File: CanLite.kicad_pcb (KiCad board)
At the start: 2 copper layers, 40 x 53.6 mm, 42 parts, among them J1 12V, J2 CAN, J3 VOLTLINK, J4 Conn_01x03, U1 LMR14006, U2 ESP32-WROOM-32D, U3 SN65HVD231, U4 BTS452T, U5 BTS452T

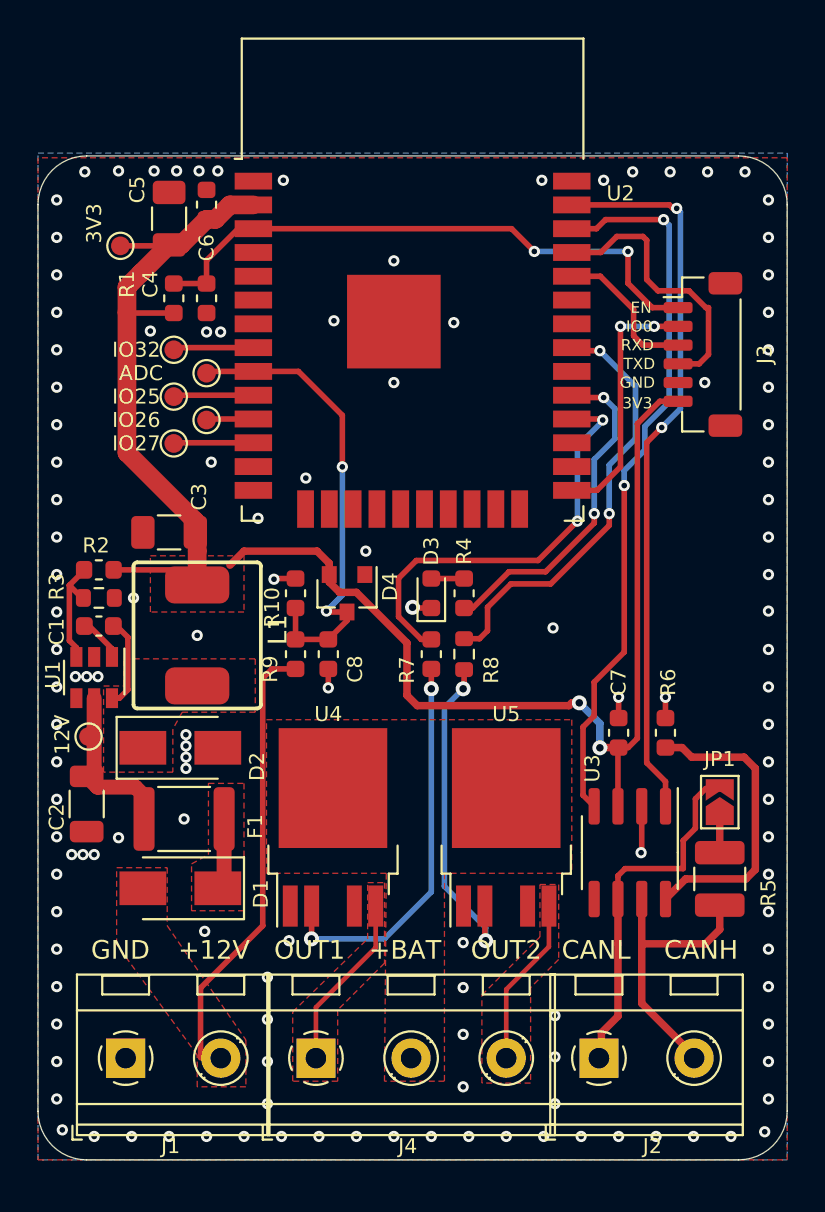
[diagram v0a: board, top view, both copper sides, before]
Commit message: Removed high side drivers, added SD card reader
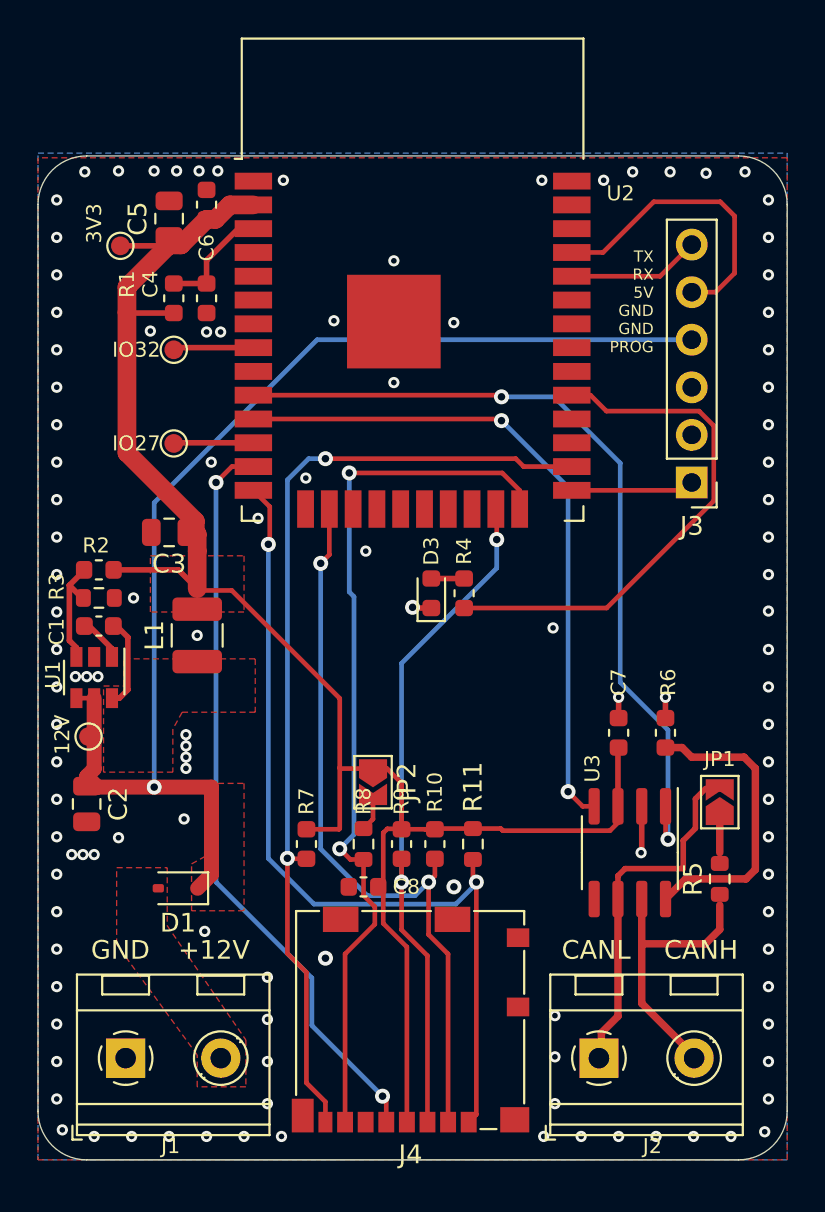
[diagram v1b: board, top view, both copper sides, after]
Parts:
- removed D2: SS14, Diode_SMD:D_SMA
- removed D4: BAS40-04, Package_TO_SOT_SMD:SOT-23
- removed F1: 0.5A, Fuse:Fuse_1812_4532Metric
- removed TP3: IO25, TestPoint:TestPoint_Pad_D1.0mm
- removed TP4: IO26, TestPoint:TestPoint_Pad_D1.0mm
- removed TP7: ADC, TestPoint:TestPoint_Pad_D1.0mm
- removed U4, U5: BTS452T, Package_TO_SOT_SMD:TO-252-4
- removed V1: VOLTLOG_LOGO, Voltlog:voltlog_mask_3mm
- added JP2: NO, Jumper:SolderJumper-2_P1.3mm_Open_TrianglePad1.0x1.5mm, F.Cu at (119.9, 84.8)
- added R11: na, Resistor_SMD:R_0603_1608Metric, F.Cu at (125.2, 88.1)
- C2, C3, C5: footprint Capacitor_SMD:C_1206_3216Metric -> Capacitor_SMD:C_0805_2012Metric
- D1: value SS14 -> 1N4148; footprint Diode_SMD:D_SMA -> Diode_SMD:D_SOD-323
- J3: value VOLTLINK -> ~; footprint Connector_JST:JST_SH_BM06B-SRSS-TB_1x06-1MP_P1.00mm_Vertical -> Connector_PinHeader_2.54mm:PinHeader_1x06_P2.54mm_Vertical
- J4: value Conn_01x03 -> Molex_104031-0811; footprint TerminalBlock_RND:TerminalBlock_RND_205-00233_1x03_P5.08mm_Horizontal -> Connector_Card:microSD_HC_Molex_104031-0811
- L1: value 8.2uH -> 4.7uH; footprint voltlog:Inductor_7.5x6.6 -> Inductor_SMD:L_1210_3225Metric
- R1, R10, R7, R8: value 10K -> 10k
- R3: value 8.45K -> 10k
- R5: footprint Resistor_SMD:R_1210_3225Metric -> Resistor_SMD:R_0603_1608Metric
- R6: value 100K -> 10K
- R9: value 36K -> 10k
- U1: value LMR14006 -> SCT2401
- moved R10 15.3 mm to (123.2, 88.1)
- moved C8 12.6 mm to (119.4, 90.4), turned to 180 degrees
- moved R7 12.1 mm to (116.3, 88.1)
- moved R9 11.6 mm to (121.4, 88.1)
- moved R8 11.5 mm to (119.4, 88.1)
- moved J3 6.86 mm to (136.9, 68.8), turned to 180 degrees
- moved J4 5.44 mm to (121.9, 97.5), turned to 180 degrees
- moved D1 0.13 mm to (109.5, 90.5)
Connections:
- C2 pad 1: Net-(C2-Pad1) -> /12V_INT
- C8 pad 1: /ADC1_CH4 -> +3V3
- D1 pad 1: Net-(D1-Pad1) -> /12V_INT
- J3 pad 1: /EN -> /IO0
- J3 pad 2: /IO0 -> GND
- J3 pad 3: /RXD -> GND
- J3 pad 4: /TXD -> /12V_INT
- J3 pad 5: GND -> /TXD
- J3 pad 6: +3V3 -> /RXD
- J4 pad 1: /OUT1 -> /IO12
- J4 pad 2: +BATT -> /IO13
- J4 pad 3: /OUT2 -> /IO15
- R10 pad 1: /ADC1_CH4 -> /IO13
- R10 pad 2: GND -> +3V3
- R7 pad 1: Net-(R7-Pad1) -> /IO4
- R7 pad 2: /CTRL1 -> +3V3
- R8 pad 1: Net-(R8-Pad1) -> /IO2
- R8 pad 2: /CTRL2 -> Net-(JP2-B)
- R9 pad 1: +12V -> /IO15
- R9 pad 2: /ADC1_CH4 -> +3V3
- TP1 pad 1: Net-(C2-Pad1) -> /12V_INT
- U1 pad 4: Net-(U1-Pad4) -> /12V_INT
- U1 pad 5: Net-(C2-Pad1) -> /12V_INT
- U2 pad 10: /IO25 -> /CAN0_TX
- U2 pad 11: /IO26 -> /CAN0_RX
- U2 pad 13: Net-(U2-Pad13) -> /IO14
- U2 pad 14: Net-(U2-Pad14) -> /IO12
- U2 pad 16: Net-(U2-Pad16) -> /IO13
- U2 pad 17: Net-(U2-Pad17) -> unconnected-(U2-SHD/SD2-Pad17)
- U2 pad 18: Net-(U2-Pad18) -> unconnected-(U2-SWP/SD3-Pad18)
- U2 pad 19: Net-(U2-Pad19) -> unconnected-(U2-SCS/CMD-Pad19)
- U2 pad 20: Net-(U2-Pad20) -> unconnected-(U2-SCK/CLK-Pad20)
- U2 pad 21: Net-(U2-Pad21) -> unconnected-(U2-SDO/SD0-Pad21)
- U2 pad 22: Net-(U2-Pad22) -> unconnected-(U2-SDI/SD1-Pad22)
- U2 pad 23: Net-(U2-Pad23) -> /IO15
- U2 pad 24: Net-(U2-Pad24) -> /IO2
- U2 pad 26: Net-(U2-Pad26) -> /IO4
- U2 pad 27: Net-(U2-Pad27) -> unconnected-(U2-IO16-Pad27)
- U2 pad 30: Net-(U2-Pad30) -> unconnected-(U2-IO18-Pad30)
- U2 pad 32: Net-(U2-Pad32) -> unconnected-(U2-NC-Pad32)
- U2 pad 33: Net-(U2-Pad33) -> unconnected-(U2-IO21-Pad33)
- U2 pad 36: /CAN0_RX -> unconnected-(U2-IO22-Pad36)
- U2 pad 37: /CAN0_TX -> unconnected-(U2-IO23-Pad37)
- U2 pad 4: Net-(U2-Pad4) -> unconnected-(U2-SENSOR_VP-Pad4)
- U2 pad 5: Net-(U2-Pad5) -> unconnected-(U2-SENSOR_VN-Pad5)
- U2 pad 6: Net-(U2-Pad6) -> unconnected-(U2-IO34-Pad6)
- U2 pad 7: Net-(U2-Pad7) -> unconnected-(U2-IO35-Pad7)
- U3 pad 5: Net-(U3-Pad5) -> unconnected-(U3-Vref-Pad5)
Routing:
- net /12V_INT: track 0.00 -> 65.4 mm, vias 0 -> 1
- net /IO4: track 0.00 -> 52.0 mm, vias 0 -> 2
- net /IO2: track 0.00 -> 47.4 mm, vias 0 -> 2
- net /IO12: track 0.00 -> 47.0 mm, vias 0 -> 2
- net /IO14: track 0.00 -> 40.3 mm, vias 0 -> 2
- net /IO13: track 0.00 -> 40.1 mm, vias 0 -> 2
- net /IO15: track 0.00 -> 36.7 mm, vias 0 -> 2
- net /ADC1_CH4: track 25.5 -> 0.00 mm, vias 2 -> 0
- net /EN: track 31.4 -> 5.94 mm, vias 2 -> 0
- net +12V: track 23.6 -> 0.00 mm
- net /CTRL2: track 23.2 -> 0.00 mm, vias 2 -> 0
- net /CTRL1: track 23.0 -> 0.00 mm, vias 2 -> 0
- net Net-(R7-Pad1): track 21.1 -> 0.00 mm, vias 2 -> 0
- net Net-(R8-Pad1): track 17.7 -> 0.00 mm, vias 2 -> 0
- net Net-(U2-IO5): track 18.0 -> 28.0 mm, vias 2 -> 0
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- added copper zone on F.Cu, net /12V_INT
- removed copper zone on F.Cu, net +BATT
- removed copper zone on F.Cu, net /OUT1
- removed copper zone on F.Cu, net /OUT2
- removed copper zone on F.Cu, net Net-(D1-Pad1)
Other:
- net class Default removed
- board text added: "TX RX 5V GND GND PROG"
- board text removed: "+BAT"
- board text removed: "ADC"
- board text removed: "EN"
- board text removed: "IO0"
- board text removed: "IO25"
- board text removed: "IO26"
- board text removed: "OUT1"
- board text removed: "OUT2"
- board text removed: "RXD"
- board text removed: "TXD"
- board text removed: "VOLTLOG"

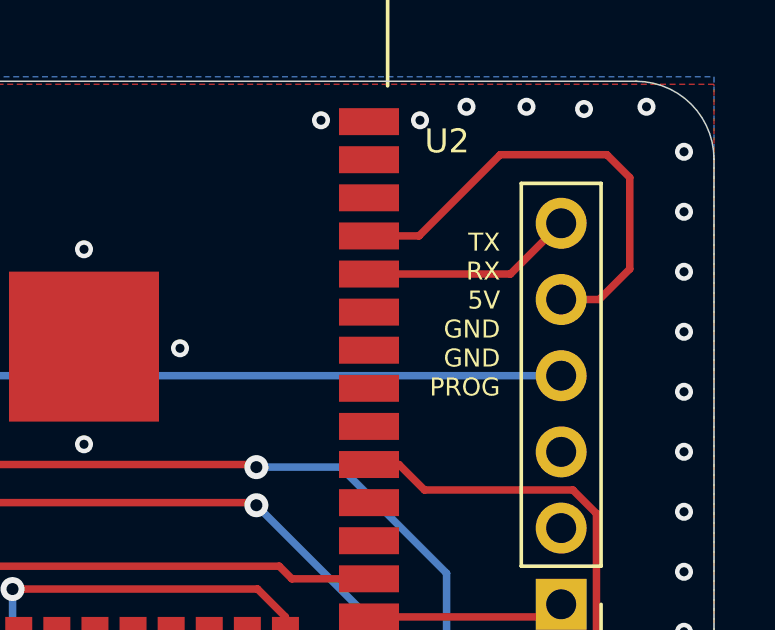
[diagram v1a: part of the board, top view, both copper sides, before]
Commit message: Silkscreen edit
Corrected pin labels on programming header
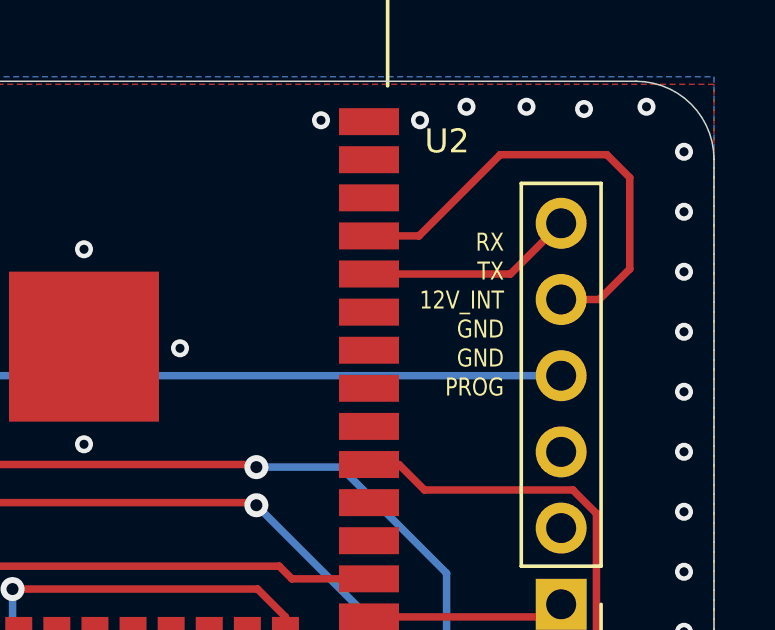
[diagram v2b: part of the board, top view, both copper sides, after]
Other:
- board text added: "RX TX 12V_INT GND GND PROG"
- board text removed: "TX RX 5V GND GND PROG"
